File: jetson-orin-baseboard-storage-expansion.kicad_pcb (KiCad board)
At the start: 2 copper layers, 27.9 x 68.6 mm, 24 parts, among them J1 J_ERM8-040-XX.X-X-DV-XX_SAMTEC

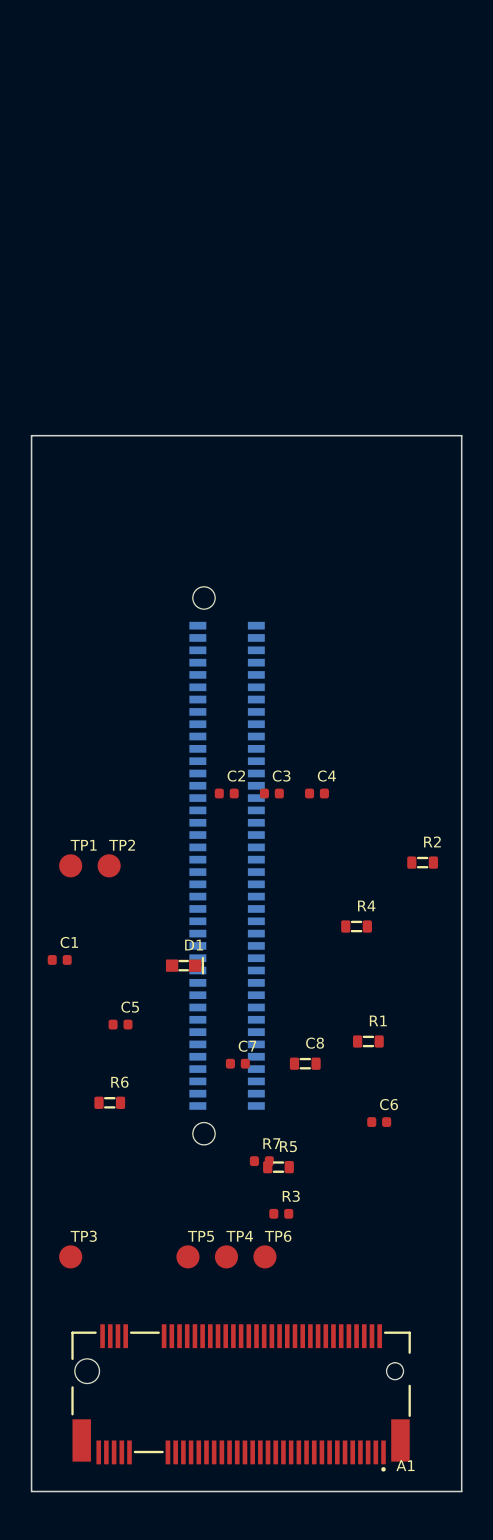
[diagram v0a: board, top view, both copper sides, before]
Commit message: [#45539] Finish schematic + draw dif pairs and other signals
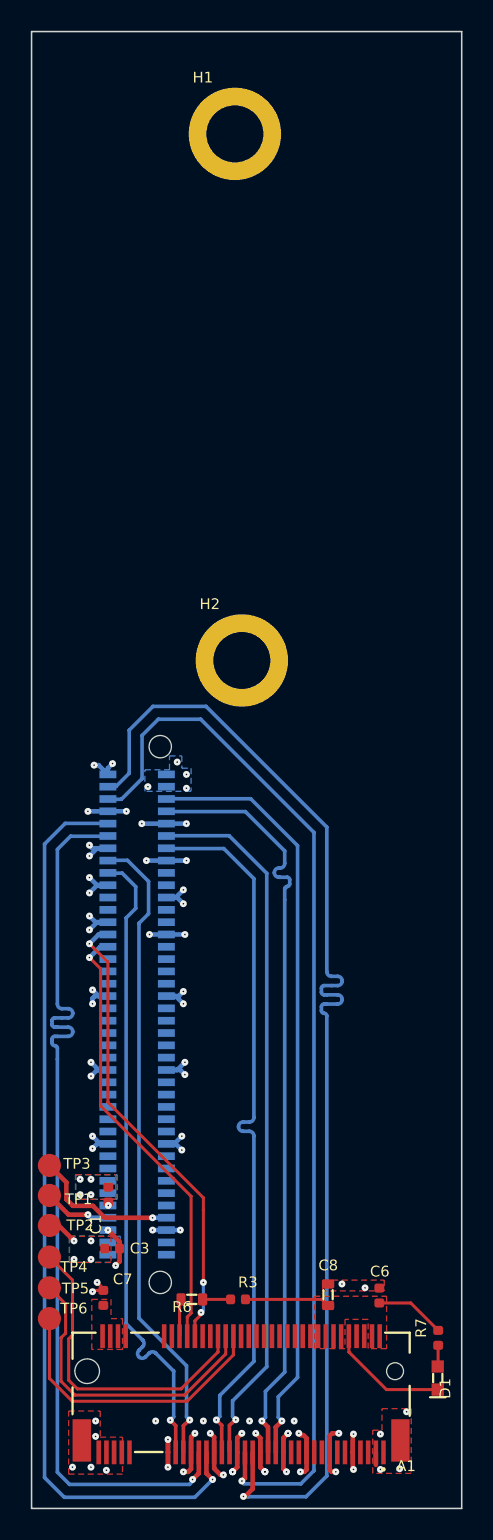
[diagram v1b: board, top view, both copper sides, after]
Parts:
- removed C2, C4, C5: C_1u_0402, antmicro-footprints:C_0402_1005Metric
- removed R1, R2, R4, R5: R_0R_0603, antmicro-footprints:R_0603_1608Metric
- added H1: Spacer_H2.5mm_9774025151, antmicro-footprints:Spacer_SMD_M2.5_H2.5mm_Wurth_9774025151, F.Cu at (66.5, 69.3)
- added H2: Spacer_H2.5mm_9774025151, antmicro-footprints:Spacer_SMD_M2.5_H2.5mm_Wurth_9774025151, F.Cu at (67.0, 103.5)
- moved D1 31.5 mm to (79.7, 150.1), turned to -90 degrees
- moved C3 31.3 mm to (58.6, 141.7), turned to 180 degrees
- moved TP2 23.7 mm to (54.5, 140.2)
- moved TP1 21.5 mm to (54.5, 138.2)
- moved C7 17.5 mm to (58.0, 144.9), turned to -90 degrees
- moved R7 16.2 mm to (79.8, 147.5), turned to 90 degrees
- moved C1 15.6 mm to (58.3, 138.2), turned to 90 degrees
- moved C8 15.1 mm to (72.6, 144.7), turned to -90 degrees
- moved TP6 14.6 mm to (54.5, 146.2)
- moved R6 13.8 mm to (63.8, 145.0), turned to 180 degrees
- moved TP4 11.5 mm to (54.5, 142.2)
- moved J1 11.3 mm to (60.2, 126.5), turned to -90 degrees
- moved C6 11.3 mm to (75.9, 144.8), turned to -90 degrees
- moved TP5 9.22 mm to (54.5, 144.2)
- moved R3 6.23 mm to (66.8, 145.0)
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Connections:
- net /Expansion Connector/1V8_CONN renamed +1V8
- net /Expansion Connector/5V_CONN renamed +5V
- A1 pad 50: /M.2/~{M2_M_PERST} -> PCIE2_RST
- A1 pad 52: /M.2/~{M2_M_CLKREQ0} -> PCIE2_CLKREQ
- C1 pad 2: /Expansion Connector/3V3_CONN -> +3V3
- J1 pad 67: /Expansion Connector/3V3_CONN -> +3V3
- J1 pad 69: /Expansion Connector/3V3_CONN -> +3V3
- J1 pad 74: Net-(C5-Pad2) -> 3V3_STDB
- J1 pad 78: /Expansion Connector/12V_CONN -> +12V
- J1 pad 80: /Expansion Connector/12V_CONN -> +12V
- TP3 pad 1: /Expansion Connector/12V_CONN -> 3V3_STDB
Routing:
- net PCIE2_TX1_N: track 0.00 -> 77.2 mm, vias 0 -> 1
- net GND: track 0.00 -> 70.5 mm, vias 0 -> 77
- net PCIE2_TX1_P: track 0.00 -> 68.8 mm, vias 0 -> 1
- net PCIE2_TX0_N: track 0.00 -> 59.7 mm, vias 0 -> 1
- net PCIE2_TX0_P: track 0.00 -> 59.6 mm, vias 0 -> 1
- net PCIE2_RX1_N: track 0.00 -> 50.0 mm, vias 0 -> 1
- net PCIE2_RX1_P: track 0.00 -> 49.9 mm, vias 0 -> 1
- net PCIE2_RX0_P: track 0.00 -> 46.3 mm, vias 0 -> 1
- net PCIE2_RX0_N: track 0.00 -> 46.3 mm, vias 0 -> 1
- net PCIE2_CLK_N: track 0.00 -> 42.2 mm, vias 0 -> 1
- net PCIE2_CLK_P: track 0.00 -> 42.1 mm, vias 0 -> 1
- net PCIE2_RST: track 0.00 -> 30.4 mm, vias 0 -> 3
- net PCIE2_CLKREQ: track 0.00 -> 28.9 mm, vias 0 -> 1
- net /M.2/~{M2_M_ALERT}: track 0.00 -> 20.7 mm
- net /M.2/M2_M_SMB_DATA: track 0.00 -> 20.0 mm
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- added copper zone on B.Cu, net +3V3
- added copper zone on F.Cu, net +3V3
- added copper zone on B.Cu, net +5V
- added copper zone on F.Cu, net +5V
- added copper zone on B.Cu, net GND
- added copper zone on F.Cu, net GND
- added copper zone on In1.Cu, net GND
- added copper zone on In2.Cu, net GND
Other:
- board size 27.9 x 68.6 mm -> 27.9 x 95.9 mm
- copper layers 2 -> 4

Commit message: [#45539] Add power traces and fix clerance DRC
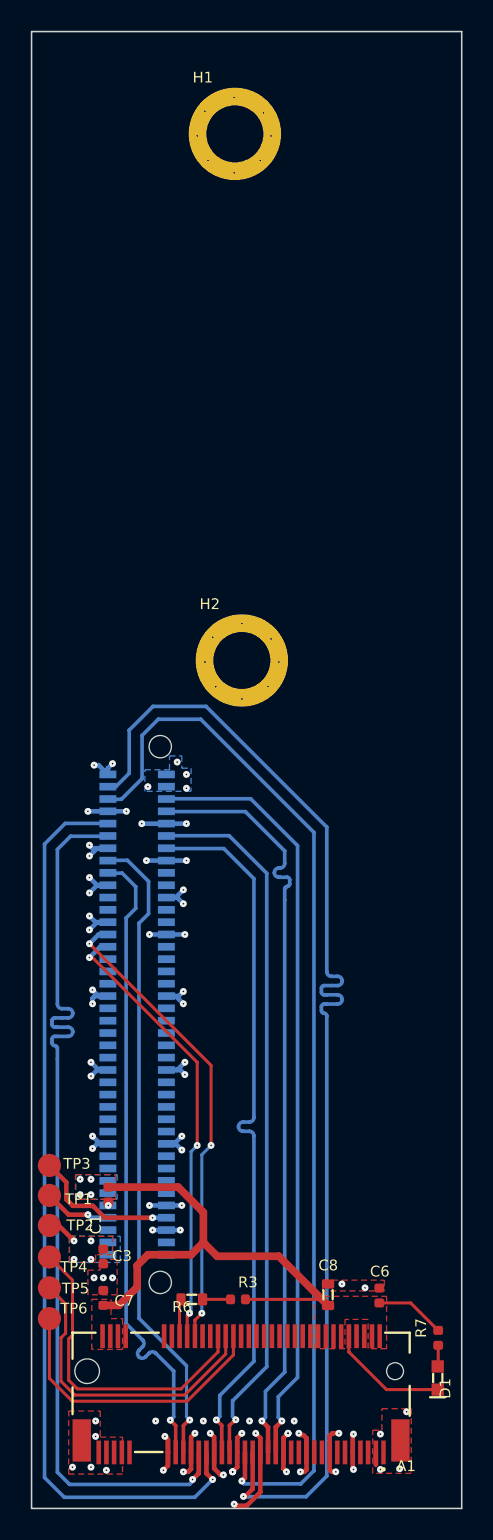
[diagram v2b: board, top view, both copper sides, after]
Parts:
- moved C3 0.77 mm to (58.0, 142.2), turned to 90 degrees
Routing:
- net +3V3: track 10.3 -> 37.7 mm
- net GND: track 70.5 -> 72.2 mm, vias 77 -> 93
- net PCIE2_CLKREQ: track 28.9 -> 29.4 mm, vias 1 -> 3

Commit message: [#45539] Fix DRC & change via size to Eurocircuits standard
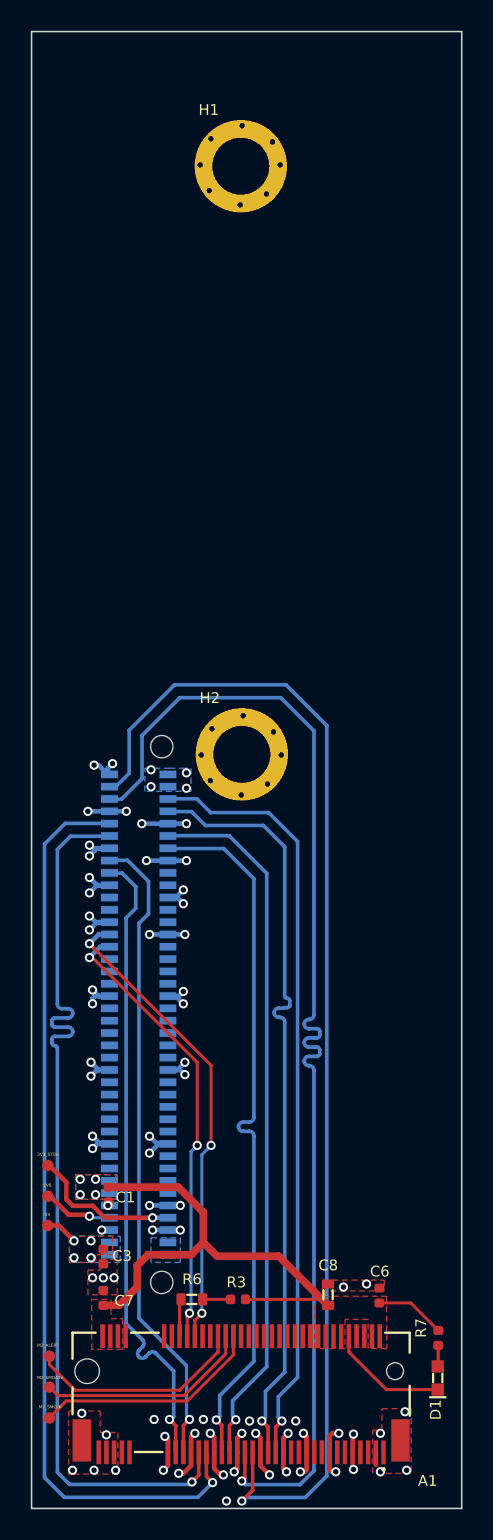
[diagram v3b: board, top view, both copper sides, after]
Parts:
- removed TP1, TP2, TP3, TP4, TP5, TP6: TP_1.5mm_SMD, antmicro-footprints:TP_SMD_1.5mm
- added 1V8: TP_0.75mm_SMD, antmicro-footprints:TP_SMD_0.75mm, F.Cu at (54.4, 138.3)
- added 3V3_STDB: TP_0.75mm_SMD, antmicro-footprints:TP_SMD_0.75mm, F.Cu at (54.4, 136.3)
- added 5V: TP_0.75mm_SMD, antmicro-footprints:TP_SMD_0.75mm, F.Cu at (54.4, 140.2)
- added M2_ALERT: TP_0.75mm_SMD, antmicro-footprints:TP_SMD_0.75mm, F.Cu at (54.5, 148.7)
- added M2_SMCLK: TP_0.75mm_SMD, antmicro-footprints:TP_SMD_0.75mm, F.Cu at (54.5, 152.7)
- added M2_SMDATA: TP_0.75mm_SMD, antmicro-footprints:TP_SMD_0.75mm, F.Cu at (54.5, 150.7)
- moved H2 6.10 mm to (67.0, 109.6)
- moved H1 2.14 mm to (66.9, 71.4)
- moved J1 0.10 mm to (60.3, 126.5)
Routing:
- net PCIE2_TX1_P: track 68.8 -> 77.5 mm
- net /M.2/~{M2_M_ALERT}: track 20.7 -> 14.2 mm
- net /M.2/M2_M_SMB_DATA: track 20.0 -> 14.0 mm
- net /M.2/M2_M_SMB_CLK: track 18.9 -> 14.9 mm
- net GND: track 72.2 -> 69.7 mm
- added copper zone on B.Cu, net +12V

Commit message: [#45539] Change spacing of the m2 spacers, fix DRC, prepare labels for sd card reader
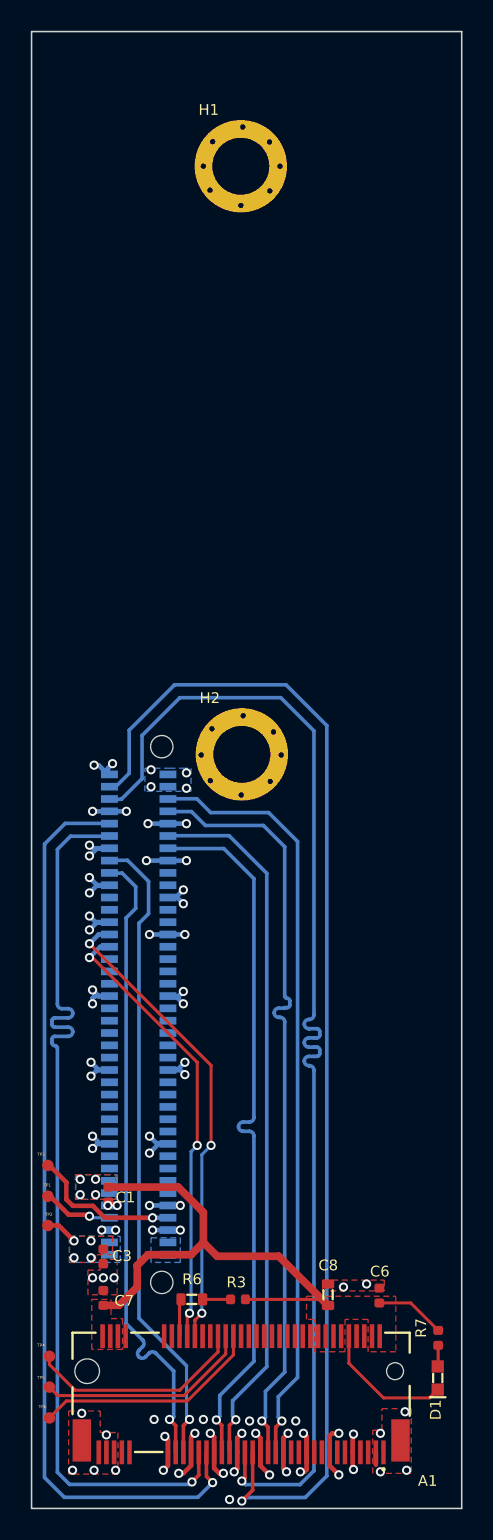
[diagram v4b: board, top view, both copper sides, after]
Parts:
- renumbered 1V8 to TP1, 5V to TP2, 3V3_STDB to TP3, M2_ALERT to TP4, M2_SMDATA to TP5, M2_SMCLK to TP6
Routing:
- net Net-(A1-Pad10): track 7.81 -> 8.69 mm
- net GND: track 69.7 -> 69.3 mm, vias 93 -> 95
